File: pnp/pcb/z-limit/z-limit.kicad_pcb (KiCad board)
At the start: 2 copper layers, 19.8 x 30.3 mm, 7 parts, among them J1 AUX, J2 HEAD_HARNESS, SW1 SW_SPDT

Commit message: adds 3d models with correct relative pathing to local library
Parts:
- moved G*** 0.10 mm to (-6.70, -3.10)
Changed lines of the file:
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@@
     (pad "5" smd roundrect (at 4 -0.5 135) (size 1 5.5) (layers "B.Cu" "B.Paste" "B.Mask") (roundrect_rratio 0.25)
       (net 5 "+3V3") (pinfunction "Pin_5") (pintype "passive"))
-    (pad "MP" smd roundrect (at -6.4 1.749999 135) (size 1.6 3) (layers "B.Cu" "B.Paste" "B.Mask") (roundrect_rratio 0.15625)
+    (pad "MP" smd roundrect (at -6.4 1.75 135) (size 1.6 3) (layers "B.Cu" "B.Paste" "B.Mask") (roundrect_rratio 0.15625)
       (net 1 "GND"))
-    (pad "MP" smd roundrect (at 6.4 1.749999 135) (size 1.6 3) (layers "B.Cu" "B.Paste" "B.Mask") (roundrect_rratio 0.15625)
+    (pad "MP" smd roundrect (at 6.4 1.75 135) (size 1.6 3) (layers "B.Cu" "B.Paste" "B.Mask") (roundrect_rratio 0.15625)
       (net 1 "GND"))
     (model "${KICAD7_3DMODEL_DIR}/Connector_JST.3dshapes/JST_PH_B5B-PH-SM4-TB_1x05-1MP_P2.00mm_Vertical.wrl"
@@
       (rotate (xyz 0 0 0))
     )
+    (model "${KIPRJMOD}/../../../lib/kicad/jst-ph.3dshapes/B5B-PH-SM4-TB.stp"
+      (offset (xyz 0 4.25 0))
+      (scale (xyz 1 1 1))
+      (rotate (xyz 0 0 0))
+    )
   )
   (footprint "index:goblin" (layer "B.Cu")
-    (at -6.7 -3 -130)
+    (at -6.7 -3.1 -130)
     (attr through_hole)
     (fp_text reference "G***" (at 0 0 50) (layer "B.SilkS") hide

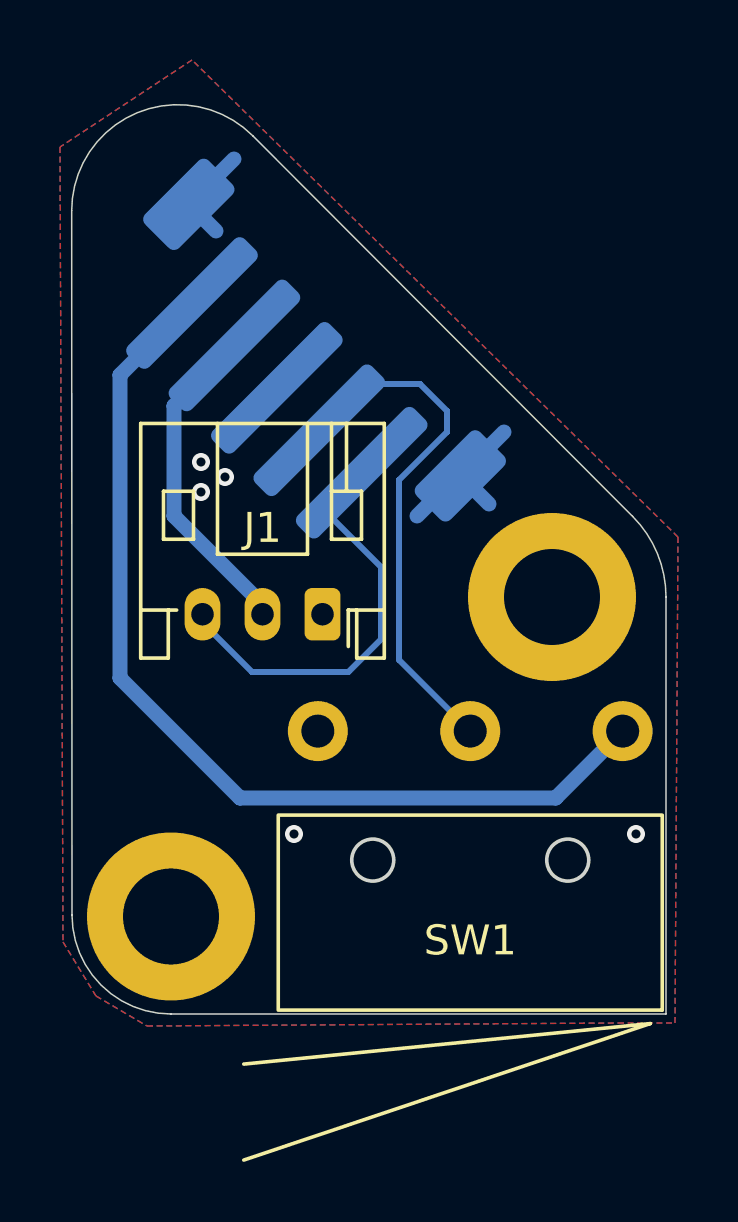
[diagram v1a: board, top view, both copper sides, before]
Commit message: adds new xy limit and rev05b1 mobo to cad
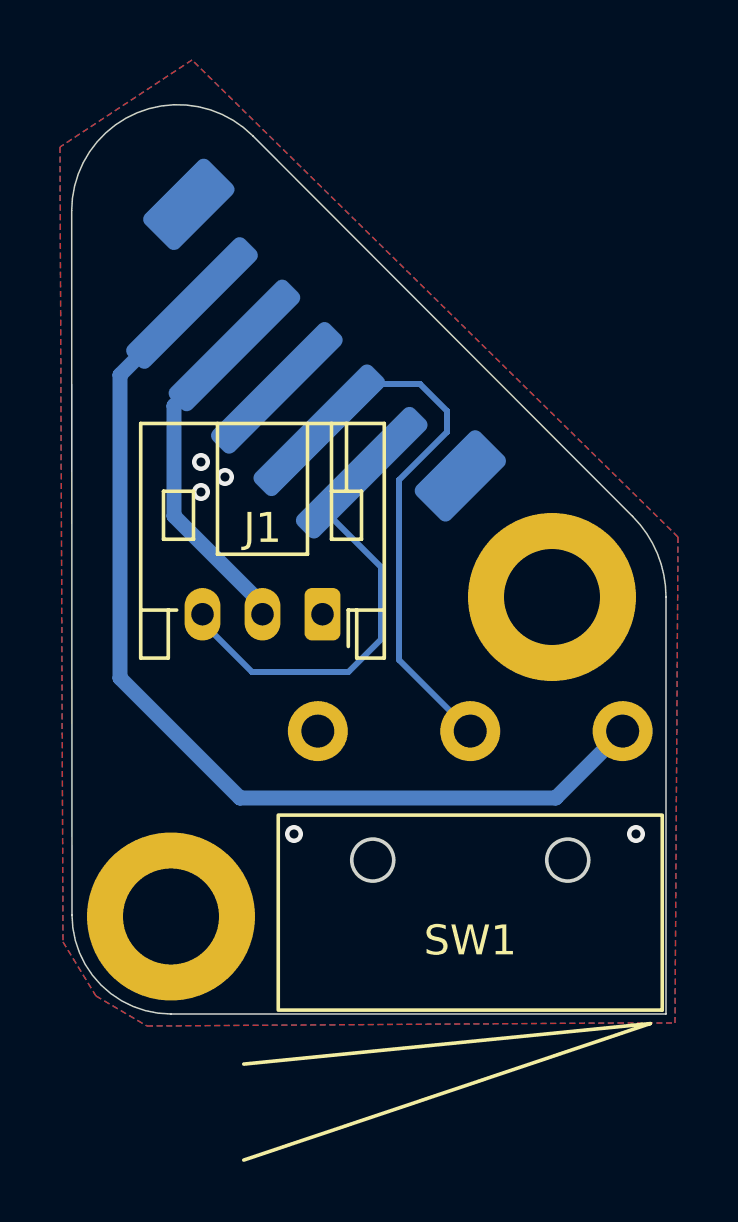
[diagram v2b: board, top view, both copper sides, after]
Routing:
- net GND: track 8.82 -> 0.16 mm
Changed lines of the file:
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@@
     (pad "5" smd roundrect (at 4 -0.5 135) (size 1 5.5) (layers "B.Cu" "B.Paste" "B.Mask") (roundrect_rratio 0.25)
       (net 5 "+3V3") (pinfunction "Pin_5") (pintype "passive"))
-    (pad "MP" smd roundrect (at -6.4 1.75 135) (size 1.6 3) (layers "B.Cu" "B.Paste" "B.Mask") (roundrect_rratio 0.15625)
-      (net 1 "GND"))
-    (pad "MP" smd roundrect (at 6.4 1.75 135) (size 1.6 3) (layers "B.Cu" "B.Paste" "B.Mask") (roundrect_rratio 0.15625)
-      (net 1 "GND"))
+    (pad "MP" smd roundrect (at -6.4 1.749999 135) (size 1.6 3) (layers "B.Cu" "B.Paste" "B.Mask") (roundrect_rratio 0.15625)
+      (net 1 "GND") (zone_connect 2))
+    (pad "MP" smd roundrect (at 6.4 1.749999 135) (size 1.6 3) (layers "B.Cu" "B.Paste" "B.Mask") (roundrect_rratio 0.15625)
+      (net 1 "GND") (zone_connect 2))
     (model "${KICAD7_3DMODEL_DIR}/Connector_JST.3dshapes/JST_PH_B5B-PH-SM4-TB_1x05-1MP_P2.00mm_Vertical.wrl"
       (offset (xyz 0 0 0))
@@
   (via (at -14.7 -17.9) (size 0.6) (drill 0.3) (layers "F.Cu" "B.Cu") (free) (net 1))
   (via (at -12.4 -6) (size 0.6) (drill 0.3) (layers "F.Cu" "B.Cu") (free) (net 1))
-  (segment (start -15.888046 -26.988046) (end -15 -26.1) (width 0.5) (layer "B.Cu") (net 1))
-  (segment (start -6.855099 -17.944901) (end -5.4 -19.4) (width 0.5) (layer "B.Cu") (net 1))
-  (segment (start -6.837079 -17.937079) (end -5.9 -17) (width 0.5) (layer "B.Cu") (net 1))
   (segment (start -6.855099 -17.937079) (end -6.855099 -17.944901) (width 0.5) (layer "B.Cu") (net 1))
   (segment (start -15.906066 -26.988046) (end -15.906066 -26.993934) (width 0.5) (layer "B.Cu") (net 1))
-  (segment (start -6.962921 -17.937079) (end -8.3 -16.6) (width 0.5) (layer "B.Cu") (net 1))
-  (segment (start -15.906066 -26.993934) (end -14.4 -28.5) (width 0.5) (layer "B.Cu") (net 1))
   (segment (start -6.855099 -17.937079) (end -6.837079 -17.937079) (width 0.5) (layer "B.Cu") (net 1))
   (segment (start -15.906066 -26.988046) (end -15.888046 -26.988046) (width 0.5) (layer "B.Cu") (net 1))

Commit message: represents REV00b1 of both xy limit and z limit boards
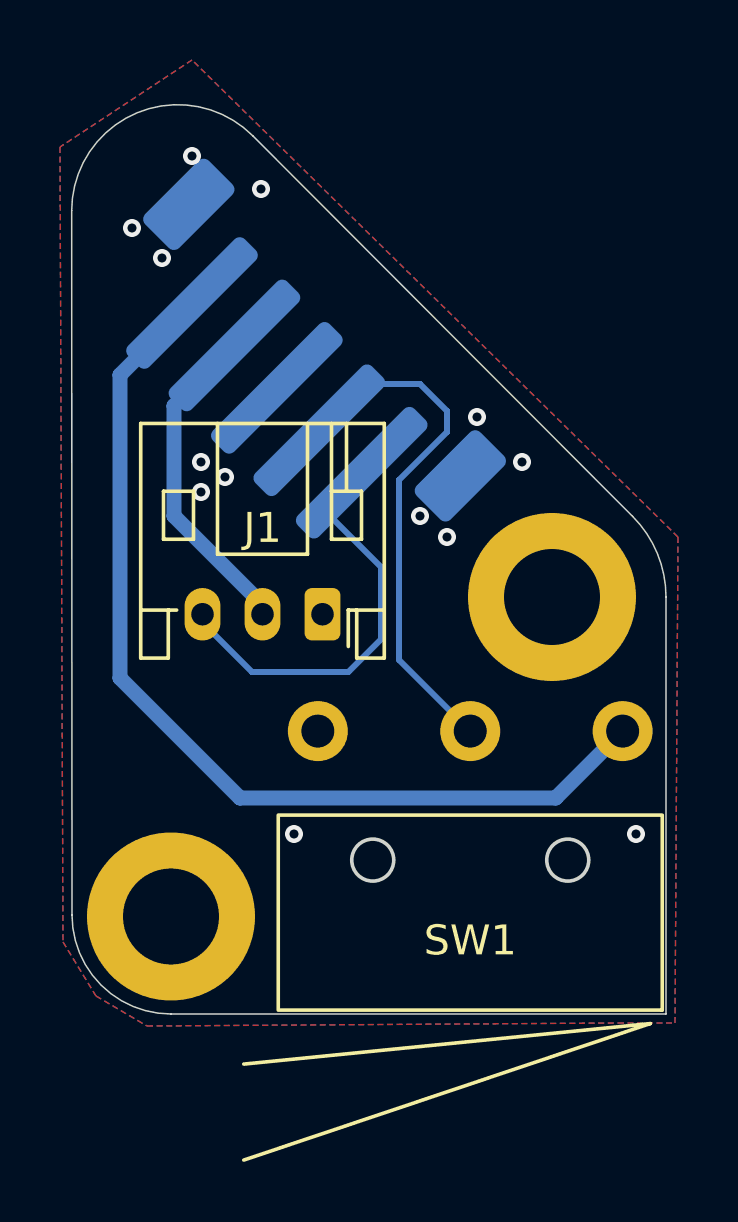
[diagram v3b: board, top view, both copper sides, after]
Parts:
- added kibuzzard-660C5135: G***, kibuzzard-660C5135, B.Cu at (-16.1, -7.50)
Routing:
- net GND: vias 5 -> 13

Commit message: updates zlimit to rev00b2 with fixed switch pinout
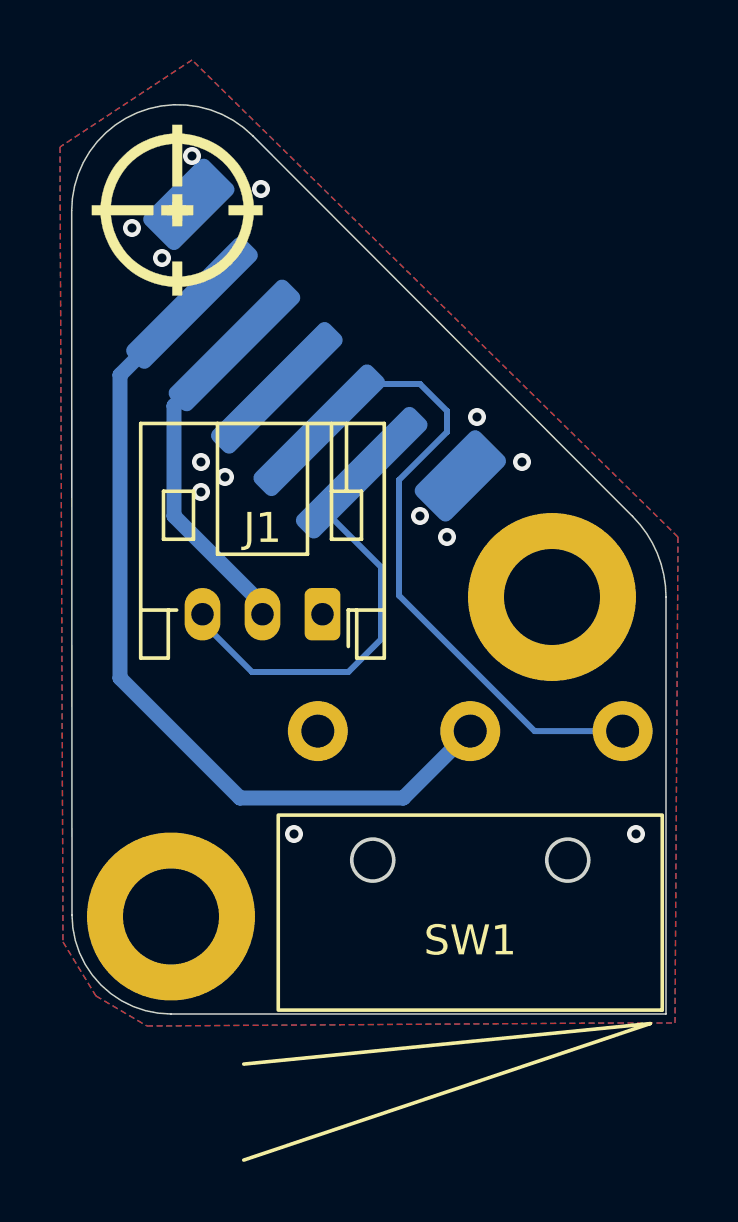
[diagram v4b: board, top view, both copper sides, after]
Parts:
- removed kibuzzard-660C5135: G***, kibuzzard-660C5135
- added kibuzzard-66478BBC: G***, kibuzzard-66478BBC, B.Cu at (-15.9, -7.45)
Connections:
- SW1 pad 1: +3V3 -> Z_LIMIT_SIG
- SW1 pad 2: Z_LIMIT_SIG -> +3V3
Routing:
- net +3V3: track 32.8 -> 27.7 mm
- net Z_LIMIT_SIG: track 17.6 -> 21.4 mm
